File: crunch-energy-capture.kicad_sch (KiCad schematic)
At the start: 0 parts

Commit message: component work mostly
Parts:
- added C1: C, Capacitor_THT:C_Rect_L18.0mm_W5.0mm_P15.00mm_FKS3_FKP3, symbol Device:C
- added C2: C, symbol Device:C
- added D1, D2, D3, D4: 600V, Diode_THT:D_DO-201AE_P15.24mm_Horizontal, symbol Diode:1.5KExxA
- added D10, D6, D7, D8, D9: 75V, Diode_THT:D_DO-35_SOD27_P7.62mm_Horizontal, symbol Device:D_Zener
- added D11: 1N5337B, Diode_THT:D_DO-201_P15.24mm_Horizontal, symbol Diode:1N53xxB
- added D12, D13: LED, Library:LED_Kingbright-SMD3528_3.5x2.8mm, symbol Device:LED
- added D5: MCR12DSNT4G, Package_TO_SOT_SMD:TO-252-2, symbol Device:Q_SCR_KAG
- added R1, R2: R, symbol Device:R
- added U1: LM3914N, Package_DIP:DIP-18_W7.62mm, symbol Driver_LED:LM3914N
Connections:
- new net: C2.1, D5.3 (G), D6.2 (A), R1.1
- new net: C2.2, D3.2 (A2), D4.2 (A2), D5.1 (K), R1.2
- new net: D11.2 (A), D13.1 (K), D5.2 (A)
- new net: D13.2 (A), R2.2
- new net: C1.2, D2.2 (A2), D4.1 (A1)
- new net: D1.1 (A1), D10.1 (K), D11.1 (K), D2.1 (A1), R2.1
- new net: D10.2 (A), D9.1 (K)
- new net: D8.1 (K), D9.2 (A)
- new net: D7.1 (K), D8.2 (A)
- new net: D6.1 (K), D7.2 (A)
- new net: C1.1, D1.2 (A2), D3.1 (A1)
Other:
- company: (none) -> Tesla Orchestra
- title: (none) -> CrunchLabs - Energy Capture Device

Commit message: bar graph first pass
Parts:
- added D14, D15, D16, D17, D18, D19, D20, D21, D22: LED, Library:LED_Kingbright-SMD3528_3.5x2.8mm, symbol Device:LED
- added R3, R4: 22K, symbol Device:R
- C2: value C -> 10nF
- R1, R2: value R -> 1K
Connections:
- net at D12.1 (K): now also U1.1 (LED1)
- net at D12.2 (A): now also D14.2 (A), D15.2 (A), D16.2 (A), D17.2 (A), D18.2 (A), D19.2 (A), D20.2 (A), D21.2 (A), D22.2 (A)
- net at U1.10 (LED10): now also D22.1 (K)
- net at U1.11 (LED9): now also D21.1 (K)
- net at U1.12 (LED8): now also D20.1 (K)
- net at U1.13 (LED7): now also D19.1 (K)
- net at U1.14 (LED6): now also D18.1 (K)
- net at U1.15 (LED5): now also D17.1 (K)
- net at U1.16 (LED4): now also D16.1 (K)
- net at U1.17 (LED3): now also D15.1 (K)
- net at U1.18 (LED2): now also D14.1 (K)
- net at U1.2 (V-): now also U1.4 (RLO), U1.8 (REFADJ), R3.2, R4.2
- net at U1.3 (V+): now also U1.9 (MODE)
- net at U1.5 (SIG): now also R4.1
- net at U1.6 (RHI): now also U1.7 (REFOUT), R3.1
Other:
- moved on the sheet: D12

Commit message: two-terminal bar graph concept
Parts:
- added D23, D24, D25, D26, D27, D28, D29, D30, D31: LED, Library:LED_Kingbright-SMD3528_3.5x2.8mm, symbol Device:LED
- added Q1: DN2470K4-G, Package_TO_SOT_SMD:TO-252-2, symbol Library:DN2470K4-G
- added R10, R11, R12, R5, R6, R7, R8, R9: 10K, Resistor_SMD:R_0805_2012Metric_Pad1.20x1.40mm_HandSolder, symbol Device:R
- added U2: SLHT50H, Package_TO_SOT_SMD:SOT-23-3, symbol Library:SLHT50H
- added U3, U4: TLV1824DR, Package_SO:SOIC-14_3.9x8.7mm_P1.27mm, symbol Library:TLV1824DR
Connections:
- new net: D27.1 (K), D28.2 (A), U4.1
- new net: R10.1, R9.2, U4.6 (-)
- new net: U3.11 (+), U3.5 (+), U3.7 (+), U3.9 (+), U4.11 (+), U4.5 (+), U4.7 (+), U4.9 (+)
- new net: R8.2, R9.1, U4.4 (-)
- new net: D29.1 (K), D30.2 (A), U4.14
- new net: R11.2, U4.8 (-)
- new net: R12.2, R5.1, U3.4 (-)
- new net: D24.1 (K), D25.2 (A), U3.13
- new net: D23.1 (K), D24.2 (A), U3.1
- new net: D28.1 (K), D29.2 (A), U4.13
- new net: D23.2 (A), D31.1 (K), U3.2
- new net: D25.1 (K), D26.2 (A), U3.14
- new net: D26.1 (K), D27.2 (A), U4.2
- new net: R7.2, R8.1, U3.8 (-)
- new net: R10.2, R11.1, U4.10 (-)
- new net: R5.2, R6.1, U3.6 (-)
- new net: R6.2, R7.1, U3.10 (-)

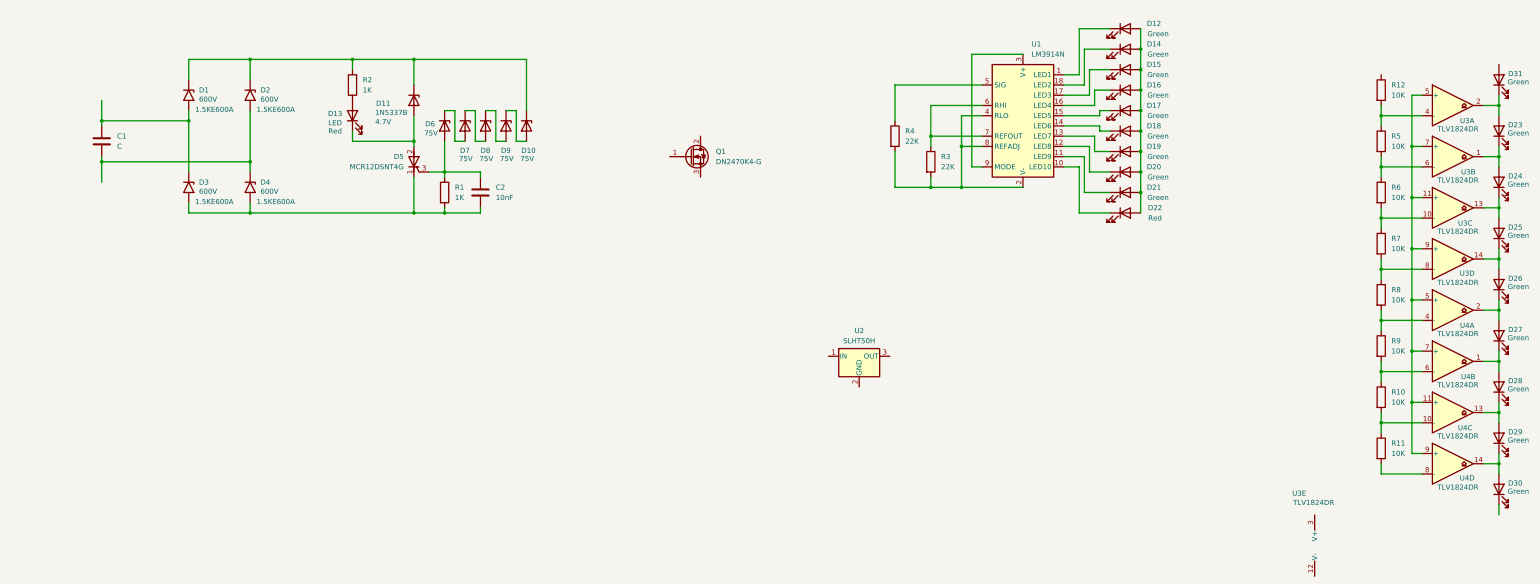
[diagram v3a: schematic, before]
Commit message: moved bar-graph to a separate project
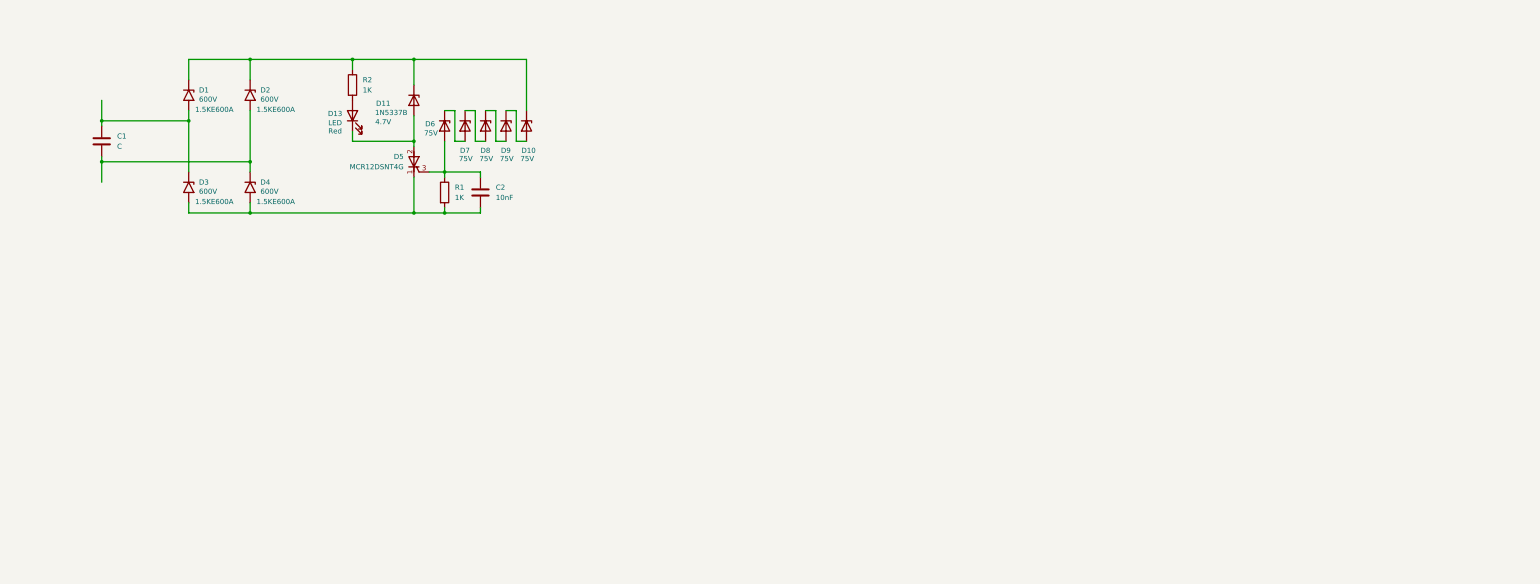
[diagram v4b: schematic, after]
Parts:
- removed D12, D14, D15, D16, D17, D18, D19, D20, D21, D22, D23, D24, D25, D26, D27, D28, D29, D30, D31: LED, Library:LED_Kingbright-SMD3528_3.5x2.8mm, symbol Device:LED
- removed Q1: DN2470K4-G, Package_TO_SOT_SMD:TO-252-2, symbol Library:DN2470K4-G
- removed R10, R11, R12, R5, R6, R7, R8, R9: 10K, Resistor_SMD:R_0805_2012Metric_Pad1.20x1.40mm_HandSolder, symbol Device:R
- removed R3, R4: 22K, symbol Device:R
- removed U1: LM3914N, Package_DIP:DIP-18_W7.62mm, symbol Driver_LED:LM3914N
- removed U2: SLHT50H, Package_TO_SOT_SMD:SOT-23-3, symbol Library:SLHT50H
- removed U3, U4: TLV1824DR, Package_SO:SOIC-14_3.9x8.7mm_P1.27mm, symbol Library:TLV1824DR

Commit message: energy capture device - work in progress
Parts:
- added C10, C5, C6, C7, C8, C9: 470uF, Capacitor_THT:CP_Radial_D35.0mm_P10.00mm_SnapIn, symbol Device:C_Polarized
- added C3, C4: 330uF, Capacitor_THT:CP_Radial_D8.0mm_P3.50mm, symbol Device:C_Polarized
- added D12: UF5408, Diode_THT:D_DO-201AD_P15.24mm_Horizontal, symbol Diode:UF5408
- added U1: EPM1210SJ, Library:EPM1210SJ_TMA, symbol Library:EPM1210SJ
- C2: footprint (none) -> Capacitor_SMD:C_0805_2012Metric_Pad1.18x1.45mm_HandSolder
- R1, R2: footprint (none) -> Resistor_SMD:R_0805_2012Metric_Pad1.20x1.40mm_HandSolder
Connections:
- net at C2.2, D3.2 (A2), D4.2 (A2)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: now also C10.2, C5.2, C6.2, C7.2, C8.2, C9.2, U1.10 (-DCIN)
- net at D1.1 (A1), D10.1 (K), D11.1 (K)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: now also D12.2 (A)
- new net: C10.1, C5.1, C6.1, C7.1, C8.1, C9.1, D12.1 (K), U1.12 (+DCIN)
- new net: C3.1, C4.1, U1.5 (+DCOUT)
- new net: C3.2, C4.2, U1.7 (-DCOUT)
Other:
- moved on the sheet: C1, C2, D1, D10, D11, D13, D2, D3, D4, D5, D6, D7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

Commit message: work in progress
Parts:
- removed D10, D6, D7, D8, D9: 75V, Diode_THT:D_DO-35_SOD27_P7.62mm_Horizontal, symbol Device:D_Zener
- added D10, D6, D7, D8, D9: BZT52B75, Diode_SMD:D_SOD-123F, symbol Diode:BZT52Bxx
- added D14: 600V, Diode_THT:D_DO-201AE_P15.24mm_Horizontal, symbol Diode:1.5KExxA
- added H1, H2: MountingHole_Pad, MountingHole:MountingHole_3.5mm_Pad_TopBottom, symbol Mechanical:MountingHole_Pad
- added H3: MountingHole, MountingHole:MountingHole_3.5mm, symbol Mechanical:MountingHole
- added J1: Input, Library:KEYSTONE_7693, symbol Connector:Screw_Terminal_01x01
- added J2: Ground, Library:KEYSTONE_7693, symbol Connector:Screw_Terminal_01x01
- added J3: Bus+, Library:KEYSTONE_7693, symbol Connector:Screw_Terminal_01x01
- added J4: Bus-, Library:KEYSTONE_7693, symbol Connector:Screw_Terminal_01x01
- added J5, J6: Screw_Terminal_01x02, TerminalBlock_MetzConnect:TerminalBlock_MetzConnect_Type011_RT05502HBLC_1x02_P5.00mm_Horizontal, symbol Connector:Screw_Terminal_01x02
- added U2: XL-4015-Buck-PCB, Library:XL4015-Buck-Module, symbol Library:XL-4015-Buck-PCB
- C1: value C -> 2.2nF
- D1, D2, D3, D4: footprint Diode_THT:D_DO-201AE_P15.24mm_Horizontal -> Diode_SMD:D_SMC_Handsoldering; Digi-Key_PN F7137CT-ND -> 18-1.5SMC600ACT-ND; MPN 1.5KE600A -> 1.5SMC600A
- D11: value 1N5337B -> 1SMB5917; footprint Diode_THT:D_DO-201_P15.24mm_Horizontal -> Diode_SMD:D_SMB_Handsoldering; Digi-Key_PN 1N5337BRLGOSCT-ND -> 1SMB5917BT3GOSCT-ND; MPN 1N5337BRLG -> 1SMB5917BT3G
- D12: value UF5408 -> MURS4100C; footprint Diode_THT:D_DO-201AD_P15.24mm_Horizontal -> Diode_SMD:D_SMC_Handsoldering; Digi-Key_PN (none) -> 31-MURS4100CCT-ND; MFG (none) -> Diodes Inc; MPN (none) -> MURS4100C
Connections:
- net BUS+: now reaches C10.1, C5.1, C6.1, C7.1, C8.1, C9.1, D12.1 (K), U1.12 (+DCIN)
- net BUS+: now also J3.1 (Pin_1)
- net RECT+: now reaches D1.1 (A1), D11.1 (K), D12.2 (A), D2.1 (A1), R2.1
- net RECT+: now also D10.1 (K)
- net at C2.1, D5.3 (G), R1.1: now also D6.2 (A)
- net BUS-: now reaches C10.2, C2.2, C5.2, C6.2, C7.2, C8.2, C9.2, D3.2 (A2), D4.2 (A2), D5.1 (K), R1.2, U1.10 (-DCIN)
- net BUS-: now also J4.1 (Pin_1)
- net IN_GND: now reaches C1.2, D2.2 (A2), D4.1 (A1)
- net IN_GND: now also H1.1, J2.1 (Pin_1)
- net 12V+: now reaches C3.1, C4.1, U1.5 (+DCOUT)
- net 12V+: now also J5.1 (Pin_1), U2.1 (+VIN)
- net 12V_GND: now reaches C3.2, C4.2, U1.7 (-DCOUT)
- net 12V_GND: now also H2.1, J5.2 (Pin_2), U2.2 (-VIN)
- net IN: now reaches C1.1, D1.2 (A2), D3.1 (A1)
- net IN: now also J1.1 (Pin_1)
- new net: D10.2 (A), D9.1 (K)
- new net: D8.1 (K), D9.2 (A)
- new net: D6.1 (K), D7.2 (A)
- new net: D7.1 (K), D8.2 (A)
- new net BAT+: J6.1 (Pin_1), U2.3 (+VOUT)
- new net BAT-: J6.2 (Pin_2), U2.4 (-VOUT)
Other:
- moved on the sheet: C10, C2, C3, C4, C5, C6, C7, C8, C9, D1, D11, D12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

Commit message: add GDT
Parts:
- removed D14: 600V, Diode_THT:D_DO-201AE_P15.24mm_Horizontal, symbol Diode:1.5KExxA
- added GD1: 350V, Diode_THT:D_5KP_P10.16mm_Horizontal, symbol Device:GDT_2Pin
- D5: value MCR12DSNT4G -> SCR
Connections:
- net BUS-: now also GD1.1
- net at D11.2 (A), D13.1 (K), D5.2 (A): now also GD1.3
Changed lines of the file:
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@@
 	)
 	(junction
+		(at 87.63 83.82)
+		(diameter 0)
+		(color 0 0 0 0)
+	)
+	(junction
 		(at 39.37 93.98)
 		(diameter 0)
@@
 	)
 	(junction
+		(at 87.63 109.22)
+		(diameter 0)
+		(color 0 0 0 0)
+	)
+	(junction
 		(at 294.64 87.63)
 		(diameter 0)
@@
 	(wire
 		(pts
+			(xy 87.63 102.87) (xy 87.63 109.22)
+		)
+		(stroke
+			(width 0)
+			(type default)
+		)
+	)
+	(wire
+		(pts
 			(xy 185.42 73.66) (xy 185.42 55.88)
 		)
@@
 	(wire
 		(pts
+			(xy 87.63 109.22) (xy 101.6 109.22)
+		)
+		(stroke
+			(width 0)
+			(type default)
+		)
+	)
+	(wire
+		(pts
 			(xy 273.05 66.04) (xy 271.78 66.04)
 		)
@@
 	(wire
 		(pts
-			(xy 66.04 109.22) (xy 101.6 109.22)
+			(xy 66.04 109.22) (xy 87.63 109.22)
 		)
 		(stroke
@@
 	(wire
 		(pts
+			(xy 87.63 83.82) (xy 87.63 92.71)
+		)
+		(stroke
+			(width 0)
+			(type default)
+		)
+	)
+	(wire
+		(pts
 			(xy 271.78 87.63) (xy 280.67 87.63)
 		)
@@
 	)
 	(symbol
+		(lib_id "Device:GDT_2Pin")
+		(at 87.63 97.79 0)
+		(unit 1)
+		(exclude_from_sim no)
+		(in_bom yes)
+		(on_board yes)
+		(dnp no)
+		(fields_autoplaced yes)
+		(property "Reference" "GD1"
+			(at 92.71 96.5199 0)
+			(effects
+				(font
+					(size 1.27 1.27)
+				)
+				(justify left)
+			)
+		)
+		(property "Value" "350V"
+			(at 92.71 99.0599 0)
+			(effects
+				(font
+					(size 1.27 1.27)
+				)
+				(justify left)
+			)
+		)
+		(property "Footprint" "Diode_THT:D_5KP_P10.16mm_Horizontal"
+			(at 87.63 97.79 90)
+			(effects
+				(font
+					(size 1.27 1.27)
+				)
+				(hide yes)
+			)
+		)
+		(property "Datasheet" "~"
+			(at 87.63 97.79 90)
+			(effects
+				(font
+					(size 1.27 1.27)
+				)
+				(hide yes)
+			)
+		)
+		(property "Description" "Gas Discharge Tube with 2 Pins"
+			(at 87.63 97.79 0)
+			(effects
+				(font
+					(size 1.27 1.27)
+				)
+				(hide yes)
+			)
+		)
+		(pin "3"
+		)
+		(pin "1"
+		)
+		(instances
+			(project "crunch-energy-capture"
+				(path "/0b60be89-a9a6-41bc-b4dc-31dfa586b7a1"
+					(reference "GD1")
+					(unit 1)
+				)
+			)
+		)
+	)
+	(symbol
 		(lib_id "Diode:BZT52Bxx")
 		(at 127 68.58 270)
@@
 			)
 		)
-		(property "Value" "MCR12DSNT4G"
+		(property "Value" "SCR"
 			(at 99.06 90.1699 0)
 			(effects
@@
 					(unit 1)
 				)
-			)
-		)
-	)
-	(symbol
-		(lib_id "Diode:1.5KExxA")
-		(at 36.83 147.32 270)
-		(unit 1)
-		(exclude_from_sim no)
-		(in_bom yes)
-		(on_board yes)
-		(dnp no)
-		(property "Reference" "D14"
-			(at 39.37 146.0499 90)
-			(effects
-				(font
-					(size 1.27 1.27)
-				)
-				(justify left)
-			)
-		)
-		(property "Value" "600V"
-			(at 39.37 148.336 90)
-			(effects
-				(font
-					(size 1.27 1.27)
-				)
-				(justify left)
-			)
-		)
-		(property "Footprint" "Diode_THT:D_DO-201AE_P15.24mm_Horizontal"
-			(at 31.75 147.32 0)
-			(effects
-				(font
-					(size 1.27 1.27)
-				)
-				(hide yes)
-			)
-		)
-		(property "Datasheet" "https://www.littelfuse.com/assetdocs/littelfuse_tvs_diode_1_5ke_datasheet.pdf?assetguid=9d02c7d2-86a5-4bff-9251-966d6af02bf7"
-			(at 36.83 146.05 0)
-			(effects
-				(font
-					(size 1.27 1.27)
-				)
-				(hide yes)
-			)
-		)
-		(property "Description" "1500W unidirectional TVS diode, DO-201AE"
-			(at 36.83 147.32 0)
-			(effects
-				(font
-					(size 1.27 1.27)
-				)
-				(hide yes)
-			)
-		)
-		(property "MFG" "LITTELFUSE INC (VA)"
-			(at 36.83 147.32 90)
-			(effects
-				(font
-					(size 1.27 1.27)
-				)
-				(hide yes)
-			)
-		)
-		(property "MPN" "1.5KE600A"
-			(at 43.18 150.876 90)
-			(effects
-				(font
-					(size 1.27 1.27)
-				)
-			)
-		)
-		(property "Digi-Key_PN" "F7137CT-ND"
-			(at 36.83 147.32 90)
-			(effects
-				(font
-					(size 1.27 1.27)
-				)
-				(hide yes)
-			)
-		)
-		(pin "1"
-		)
-		(pin "2"
-		)
-		(instances
-			(project "crunch-energy-capture"
-				(path "/0b60be89-a9a6-41bc-b4dc-31dfa586b7a1"
-					(reference "D14")
-					(unit 1)
-				)

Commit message: finished layout and ordered
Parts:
- added H4: MountingHole_Pad, MountingHole:MountingHole_3.5mm_Pad_TopBottom, symbol Mechanical:MountingHole_Pad
- GD1: footprint Diode_THT:D_5KP_P10.16mm_Horizontal -> Library:GDT_Bourns_2053_SM; Digi-Key_PN (none) -> 118-2053-35-SM-RPLFCT-ND; MFG (none) -> Bourns, Inc; MPN (none) -> 2053-35-SM-RPLF
- renumbered H3 to H2, H2 to H3
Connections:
- net 12V_GND: now also H4.1
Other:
- moved on the sheet: H2
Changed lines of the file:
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@@
 			)
 		)
-		(property "Footprint" "Diode_THT:D_5KP_P10.16mm_Horizontal"
+		(property "Footprint" "Library:GDT_Bourns_2053_SM"
 			(at 87.63 97.79 90)
 			(effects
@@
 			)
 		)
-		(property "Datasheet" "~"
+		(property "Datasheet" "https://www.bourns.com/docs/Product-Datasheets/2053.pdf"
 			(at 87.63 97.79 90)
 			(effects
@@
 		)
 		(property "Description" "Gas Discharge Tube with 2 Pins"
+			(at 87.63 97.79 0)
+			(effects
+				(font
+					(size 1.27 1.27)
+				)
+				(hide yes)
+			)
+		)
+		(property "MFG" "Bourns, Inc"
+			(at 87.63 97.79 0)
+			(effects
+				(font
+					(size 1.27 1.27)
+				)
+				(hide yes)
+			)
+		)
+		(property "MPN" "2053-35-SM-RPLF"
+			(at 87.63 97.79 0)
+			(effects
+				(font
+					(size 1.27 1.27)
+				)
+				(hide yes)
+			)
+		)
+		(property "Digi-Key_PN" "118-2053-35-SM-RPLFCT-ND"
 			(at 87.63 97.79 0)
 			(effects
@@
 	(symbol
 		(lib_id "Mechanical:MountingHole")
-		(at 281.94 116.84 0)
+		(at 39.37 118.11 0)
 		(unit 1)
 		(exclude_from_sim no)
@@
 		(on_board yes)
 		(dnp no)
-		(fields_autoplaced yes)
-		(property "Reference" "H3"
-			(at 284.48 115.5699 0)
+		(property "Reference" "H2"
+			(at 34.036 116.84 0)
 			(effects
 				(font
@@
 		)
 		(property "Value" "MountingHole"
-			(at 284.48 118.1099 0)
-			(effects
-				(font
-					(size 1.27 1.27)
-				)
-				(justify left)
+			(at 41.91 119.3799 0)
+			(effects
+				(font
+					(size 1.27 1.27)
+				)
+				(justify left)
+				(hide yes)
 			)
 		)
 		(property "Footprint" "MountingHole:MountingHole_3.5mm"
-			(at 281.94 116.84 0)
+			(at 39.37 118.11 0)
 			(effects
 				(font
@@
 		)
 		(property "Datasheet" "~"
-			(at 281.94 116.84 0)
+			(at 39.37 118.11 0)
 			(effects
 				(font
@@
 		)
 		(property "Description" "Mounting Hole without connection"
-			(at 281.94 116.84 0)
-			(effects
-				(font
-					(size 1.27 1.27)
-				)
-				(hide yes)
-			)
-		)
-		(instances
-			(project "crunch-energy-capture"
-				(path "/0b60be89-a9a6-41bc-b4dc-31dfa586b7a1"
-					(reference "H3")
+			(at 39.37 118.11 0)
+			(effects
+				(font
+					(size 1.27 1.27)
+				)
+				(hide yes)
+			)
+		)
+		(instances
+			(project "crunch-energy-capture"
+				(path "/0b60be89-a9a6-41bc-b4dc-31dfa586b7a1"
+					(reference "H2")
 					(unit 1)
 				)
@@
 				)
 				(justify right)
+				(hide yes)
 			)
 		)
@@
 		(dnp no)
 		(fields_autoplaced yes)
-		(property "Reference" "H2"
+		(property "Reference" "H3"
 			(at 278.13 90.1699 0)
 			(effects
@@
 				)
 				(justify right)
+				(hide yes)
 			)
 		)
@@
 			(project "crunch-energy-capture"
 				(path "/0b60be89-a9a6-41bc-b4dc-31dfa586b7a1"
-					(reference "H2")
+					(reference "H3")
 					(unit 1)
 				)
@@
 					(unit 1)
 				)
+			)
+		)
+	)
+	(symbol
+		(lib_id "Mechanical:MountingHole_Pad")
+		(at 294.64 90.17 0)
+		(mirror x)
+		(unit 1)
+		(exclude_from_sim no)
+		(in_bom no)
+		(on_board yes)
+		(dnp no)
+		(fields_autoplaced yes)
+		(property "Reference" "H4"
+			(at 292.1 90.1699 0)
+			(effects
+				(font
+					(size 1.27 1.27)
+				)
+				(justify right)
+			)
+		)
+		(property "Value" "MountingHole_Pad"
+			(at 292.1 92.7099 0)
+			(effects
+				(font
+					(size 1.27 1.27)
+				)
+				(justify right)
+				(hide yes)
+			)
+		)
+		(property "Footprint" "MountingHole:MountingHole_3.5mm_Pad_TopBottom"
+			(at 294.64 90.17 0)
+			(effects
+				(font
+					(size 1.27 1.27)
+				)
+				(hide yes)
+			)
+		)
+		(property "Datasheet" "~"
+			(at 294.64 90.17 0)
+			(effects
+				(font
+					(size 1.27 1.27)
+				)
+				(hide yes)
+			)
+		)
+		(property "Description" "Mounting Hole with connection"
+			(at 294.64 90.17 0)
+			(effects
+				(font
+					(size 1.27 1.27)
+				)
+				(hide yes)
+			)
+		)
+		(pin "1"
+		)
+		(instances
+			(project "crunch-energy-capture"
+				(path "/0b60be89-a9a6-41bc-b4dc-31dfa586b7a1"
+					(reference "H4")
+					(unit 1)
+				)
